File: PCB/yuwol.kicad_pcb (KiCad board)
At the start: 2 copper layers, 172.5 x 122.5 mm, 3 parts

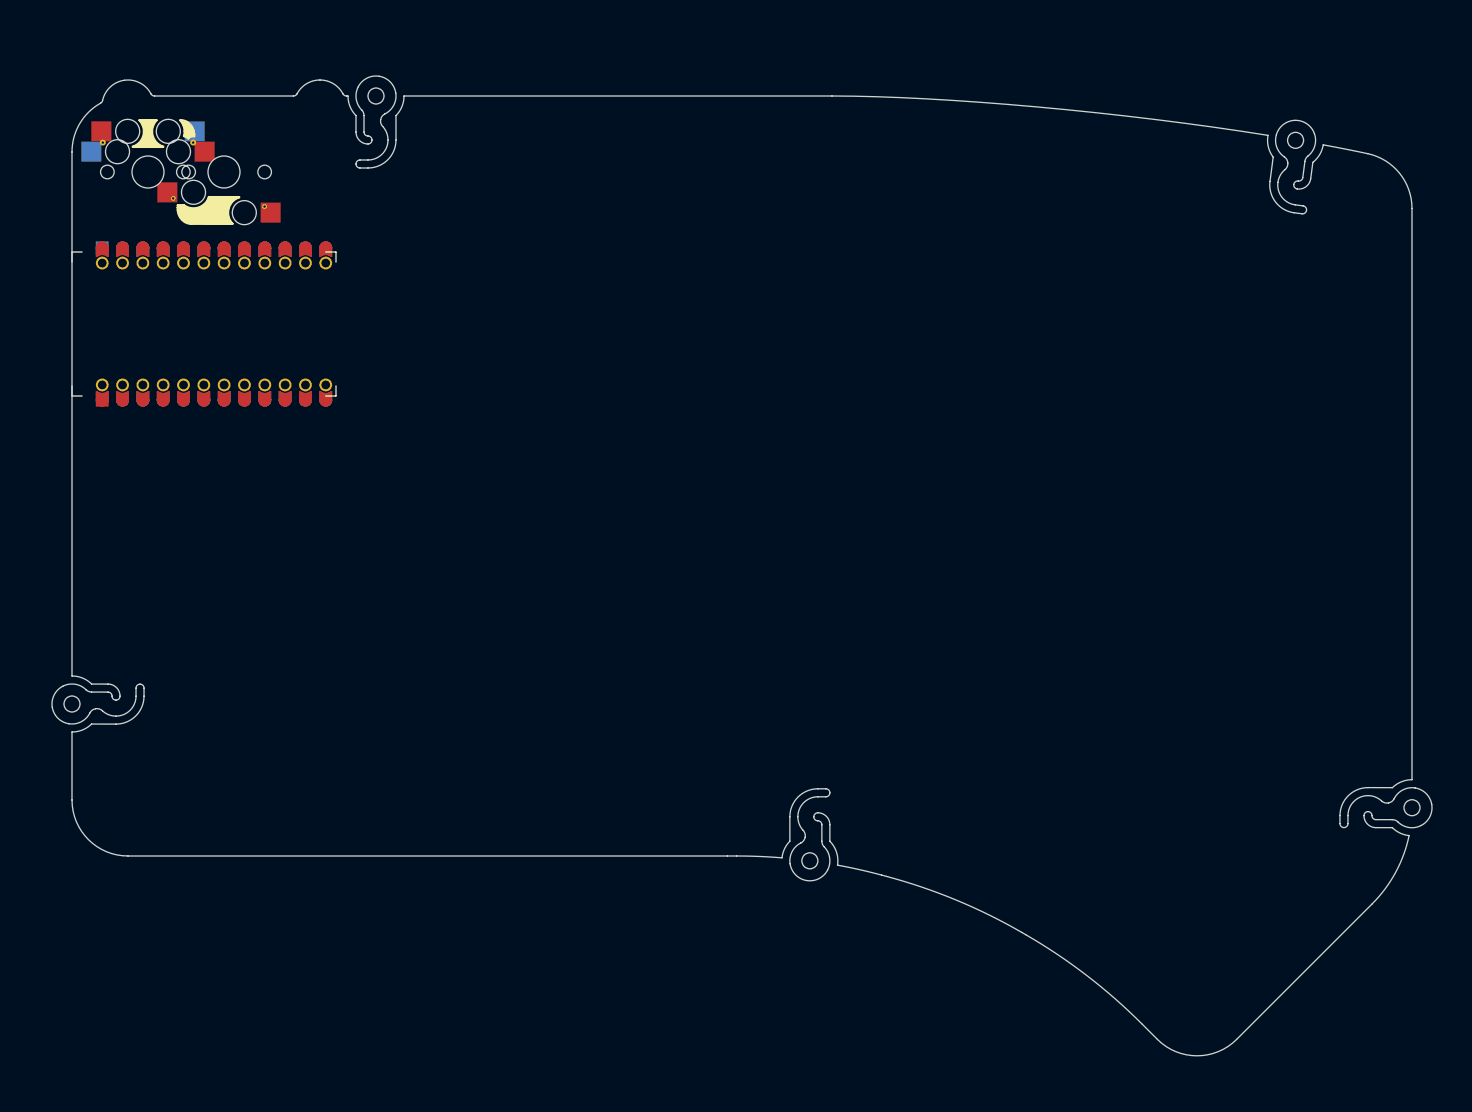
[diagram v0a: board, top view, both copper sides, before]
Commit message: place components
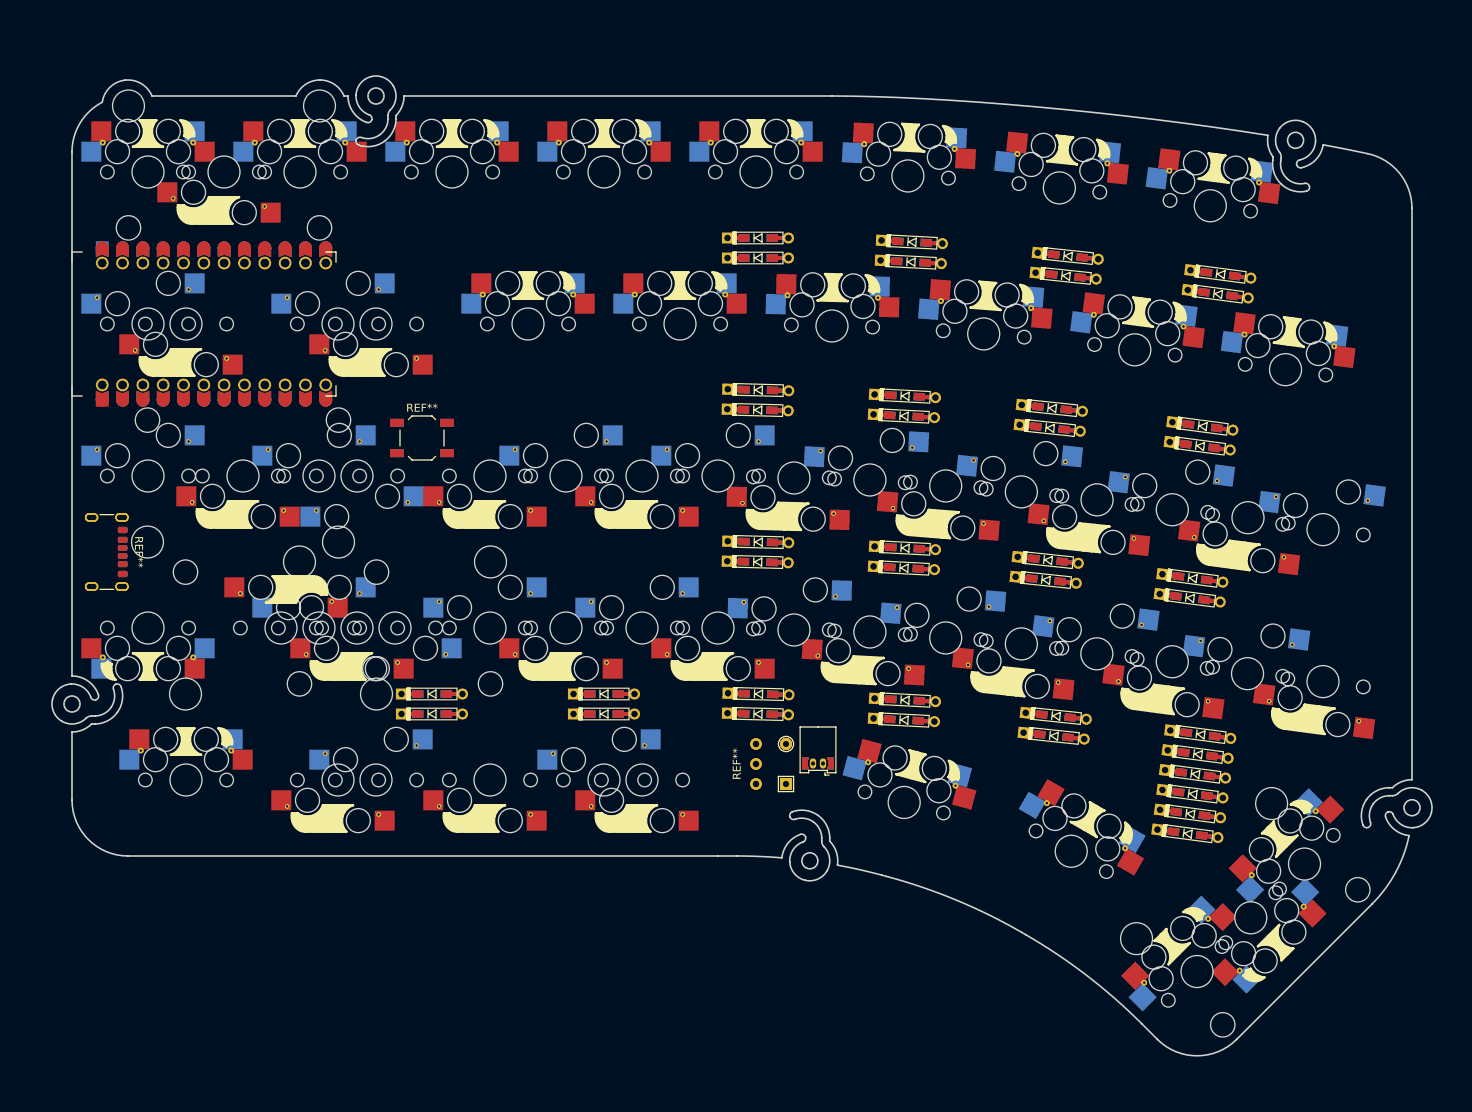
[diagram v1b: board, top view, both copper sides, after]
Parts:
- added REF**: TestPoint_THTPad_D1.5mm_Drill0.7mm, TestPoint:TestPoint_THTPad_D1.5mm_Drill0.7mm, F.Cu at (151.2, 121.0)
- added REF**: D, yubuGadgetsFootpints:Diode_TH_SMD_REVERSIBLE, F.Cu at (184.7, 120.0)
- added REF**: D, yubuGadgetsFootpints:Diode_TH_SMD_REVERSIBLE, F.Cu at (166.0, 118.0)
- added REF**: D, yubuGadgetsFootpints:Diode_TH_SMD_REVERSIBLE, F.Cu at (203.3, 81.3)
- added REF**: D, yubuGadgetsFootpints:Diode_TH_SMD_REVERSIBLE, F.Cu at (202.7, 122.3)
- added REF**: D, yubuGadgetsFootpints:Diode_TH_SMD_REVERSIBLE, F.Cu at (186.2, 62.5)
- added REF**: D, yubuGadgetsFootpints:Diode_TH_SMD_REVERSIBLE, F.Cu at (166.9, 60.7)
- added REF**: D, yubuGadgetsFootpints:Diode_TH_SMD_REVERSIBLE, F.Cu at (147.8, 76.8)
- added REF**: D, yubuGadgetsFootpints:Diode_TH_SMD_REVERSIBLE, F.Cu at (147.8, 60.2)
- added REF**: D, yubuGadgetsFootpints:Diode_TH_SMD_REVERSIBLE, F.Cu at (128.5, 114.8)
- added REF**: StabilizerHole_2u, yubuGadgetsFootpints:StabilizerHole_2u, F.Cu at (88.1, 106.5)
- added REF**: D, yubuGadgetsFootpints:Diode_TH_SMD_REVERSIBLE, F.Cu at (166.1, 115.5)
- added REF**: TestPoint_THTPad_1.5x1.5mm_Drill0.7mm, TestPoint:TestPoint_THTPad_1.5x1.5mm_Drill0.7mm, F.Cu at (151.2, 126.0)
- added REF**: D, yubuGadgetsFootpints:Diode_TH_SMD_REVERSIBLE, F.Cu at (184.0, 98.0)
- added REF**: D, yubuGadgetsFootpints:Diode_TH_SMD_REVERSIBLE, F.Cu at (107.0, 114.8)
- added REF**: D, yubuGadgetsFootpints:Diode_TH_SMD_REVERSIBLE, F.Cu at (183.7, 100.5)
- added REF**: D, yubuGadgetsFootpints:Diode_TH_SMD_REVERSIBLE, F.Cu at (147.8, 57.8)
- added REF**: D, yubuGadgetsFootpints:Diode_TH_SMD_REVERSIBLE, F.Cu at (147.8, 114.8)
- added REF**: D, yubuGadgetsFootpints:Diode_TH_SMD_REVERSIBLE, F.Cu at (107.0, 117.2)
- added REF**: D, yubuGadgetsFootpints:Diode_TH_SMD_REVERSIBLE, F.Cu at (205.6, 62.3)
- added REF**: D, yubuGadgetsFootpints:Diode_TH_SMD_REVERSIBLE, F.Cu at (128.5, 117.2)
- added REF**: D, yubuGadgetsFootpints:Diode_TH_SMD_REVERSIBLE, F.Cu at (147.8, 95.8)
- added REF**: USB_C_Receptacle_GCT_USB4125-xx-x_6P_TopMnt_Horizontal, Connector_USB:USB_C_Receptacle_GCT_USB4125-xx-x_6P_TopMnt_Horizontal, F.Cu at (65.2, 97.0)
- added REF**: D, yubuGadgetsFootpints:Diode_TH_SMD_REVERSIBLE, F.Cu at (185.0, 117.5)
- added REF**: D, yubuGadgetsFootpints:Diode_TH_SMD_REVERSIBLE, F.Cu at (202.4, 124.8)
- added REF**: Molex_PicoBlade_53048-0210_1x02_P1.25mm_Horizontal_Reversib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, yubuGadgetsFootpints:Molex_PicoBlade_53048-0210_1x02_P1.25mm_Horizontal_ReversibleThru, F.Cu at (155.2, 121.8)
- added REF**: D, yubuGadgetsFootpints:Diode_TH_SMD_REVERSIBLE, F.Cu at (203.1, 119.8)
- added REF**: D, yubuGadgetsFootpints:Diode_TH_SMD_REVERSIBLE, F.Cu at (166.0, 80.0)
- added REF**: D, yubuGadgetsFootpints:Diode_TH_SMD_REVERSIBLE, F.Cu at (184.2, 81.5)
- added REF**: D, yubuGadgetsFootpints:Diode_TH_SMD_REVERSIBLE, F.Cu at (147.7, 98.2)
- added REF**: StabilizerHole_2u, yubuGadgetsFootpints:StabilizerHole_2u, F.Cu at (102.4, 106.5)
- added REF**: D, yubuGadgetsFootpints:Diode_TH_SMD_REVERSIBLE, F.Cu at (166.1, 77.5)
- added REF**: D, yubuGadgetsFootpints:Diode_TH_SMD_REVERSIBLE, F.Cu at (166.0, 99.0)
- added REF**: D, yubuGadgetsFootpints:Diode_TH_SMD_REVERSIBLE, F.Cu at (186.5, 60.0)
- added REF**: D, yubuGadgetsFootpints:Diode_TH_SMD_REVERSIBLE, F.Cu at (201.5, 132.2)
- added REF**: D, yubuGadgetsFootpints:Diode_TH_SMD_REVERSIBLE, F.Cu at (147.7, 79.2)
- added REF**: D, yubuGadgetsFootpints:Diode_TH_SMD_REVERSIBLE, F.Cu at (201.8, 129.7)
- added REF**: D, yubuGadgetsFootpints:Diode_TH_SMD_REVERSIBLE, F.Cu at (205.2, 64.8)
- added REF**: SW_SPDT_SS-12D00, yubuGadgetsFootpints:SW_SPDT_SS-12D00, F.Cu at (147.5, 123.5)
- added REF**: StabilizerHole_2u, yubuGadgetsFootpints:StabilizerHole_2u, F.Cu at (81.0, 49.5)
- added REF**: StabilizerHole_2u, yubuGadgetsFootpints:StabilizerHole_2u, F.Cu at (209.3, 142.7)
- added REF**: D, yubuGadgetsFootpints:Diode_TH_SMD_REVERSIBLE, F.Cu at (147.8, 117.2)
- added REF**: D, yubuGadgetsFootpints:Diode_TH_SMD_REVERSIBLE, F.Cu at (201.8, 102.8)
- added REF**: SW_SPST_TL3342, Button_Switch_SMD:SW_SPST_TL3342, F.Cu at (105.8, 82.8)
- added REF**: D, yubuGadgetsFootpints:Diode_TH_SMD_REVERSIBLE, F.Cu at (166.1, 96.5)
- added REF**: D, yubuGadgetsFootpints:Diode_TH_SMD_REVERSIBLE, F.Cu at (203.0, 83.8)
- added REF**: StabilizerHole_2u, yubuGadgetsFootpints:StabilizerHole_2u, F.Cu at (83.4, 87.5)
- added REF**: TestPoint_THTPad_D1.5mm_Drill0.7mm, TestPoint:TestPoint_THTPad_D1.5mm_Drill0.7mm, B.Cu at (151.2, 121.0)
- added REF**: USB_C_Receptacle_GCT_USB4125-xx-x_6P_TopMnt_Horizontal, Connector_USB:USB_C_Receptacle_GCT_USB4125-xx-x_6P_TopMnt_Horizontal, B.Cu at (65.2, 97.0)
- added REF**: TestPoint_THTPad_1.5x1.5mm_Drill0.7mm, TestPoint:TestPoint_THTPad_1.5x1.5mm_Drill0.7mm, B.Cu at (151.2, 126.0)
- added REF**: SW_SPST_TL3342, Button_Switch_SMD:SW_SPST_TL3342, B.Cu at (105.8, 82.8)
- added REF**: D, yubuGadgetsFootpints:Diode_TH_SMD_REVERSIBLE, F.Cu at (202.1, 100.3)
- added REF**: D, yubuGadgetsFootpints:Diode_TH_SMD_REVERSIBLE, F.Cu at (184.5, 79.0)
- added REF**: D, yubuGadgetsFootpints:Diode_TH_SMD_REVERSIBLE, F.Cu at (167.0, 58.2)
- added REF**: D, yubuGadgetsFootpints:Diode_TH_SMD_REVERSIBLE, F.Cu at (202.1, 127.2)
- added S*: Val**, yubuGadgetsFootpints:MX_Hotswap_FootprintPropertyFix_Guided, F.Cu at (204.3, 53.7)
- added S*: Val**, yubuGadgetsFootpints:MX_Hotswap_FootprintPropertyFix_Guided, F.Cu at (186.9, 134.4)
- added S*: Val**, yubuGadgetsFootpints:MX_Hotswap_FootprintPropertyFix_Guided, F.Cu at (71.5, 106.5)
- added S*: Val**, yubuGadgetsFootpints:MX_Hotswap_FootprintPropertyFix_Guided, F.Cu at (176.0, 69.7)
- added S*: Val**, yubuGadgetsFootpints:MX_Hotswap_FootprintPropertyFix_Guided, F.Cu at (166.5, 50.0)
- added S*: Val**, yubuGadgetsFootpints:MX_HotswapOneside_Via_Guided, F.Cu at (180.7, 108.5)
- added S*: Val**, yubuGadgetsFootpints:MX_Hotswap_FootprintPropertyFix_Guided, F.Cu at (157.0, 68.7)
- added S*: Val**, yubuGadgetsFootpints:MX_HotswapOneside_Via_Guided, F.Cu at (171.2, 88.7)
- added S*: Val**, yubuGadgetsFootpints:MX_Hotswap_FootprintPropertyFix_Guided, F.Cu at (90.5, 49.5)
- added S*: Val**, yubuGadgetsFootpints:MX_HotswapOneside_Via_Guided, F.Cu at (123.8, 106.5)
- added S*: Val**, yubuGadgetsFootpints:MX_Hotswap_FootprintPropertyFix_Guided, F.Cu at (213.7, 74.2)
- added S*: Val**, yubuGadgetsFootpints:MX_HotswapOneside_Via_Guided, F.Cu at (114.2, 125.5)
- added S*: Val**, yubuGadgetsFootpints:MX_Hotswap_FootprintPropertyFix_Guided, F.Cu at (138.0, 68.5)
- added S*: Val**, yubuGadgetsFootpints:MX_Hotswap_FootprintPropertyFix_Guided, F.Cu at (76.2, 125.5)
- added S*: Val**, yubuGadgetsFootpints:MX_HotswapOneside_Via_Guided, F.Cu at (76.2, 68.5)
- added S*: Val**, yubuGadgetsFootpints:MX_HotswapOneside_Via_Guided, F.Cu at (190.1, 90.5)
- added S*: Val**, yubuGadgetsFootpints:MX_HotswapOneside_Via_Guided, F.Cu at (218.4, 113.2)
- added S*: Val**, yubuGadgetsFootpints:MX_Hotswap_FootprintPropertyFix_Guided, F.Cu at (209.3, 142.7)
- added S*: Val**, yubuGadgetsFootpints:MX_HotswapOneside_Via_Guided, F.Cu at (142.8, 106.5)
- added S*: Val**, yubuGadgetsFootpints:MX_HotswapOneside_Via_Guided, F.Cu at (152.2, 87.7)
- added S*: Val**, yubuGadgetsFootpints:MX_Hotswap_FootprintPropertyFix_Guided, F.Cu at (202.6, 149.4)
- added S*: Val**, yubuGadgetsFootpints:MX_HotswapOneside_Via_Guided, F.Cu at (97.6, 106.5)
- added S*: Val**, yubuGadgetsFootpints:MX_HotswapOneside_Via_Guided, F.Cu at (209.0, 92.7)
- added S*: Val**, yubuGadgetsFootpints:MX_Hotswap_FootprintPropertyFix_Guided, F.Cu at (119.0, 68.5)
- added S*: Val**, yubuGadgetsFootpints:MX_Hotswap_FootprintPropertyFix_Guided, F.Cu at (166.0, 128.3)
- added S*: Val**, yubuGadgetsFootpints:MX_HotswapOneside_Via_Guided, F.Cu at (133.2, 125.5)
- added S*: Val**, yubuGadgetsFootpints:MX_HotswapOneside_Via_Guided, F.Cu at (88.1, 106.5)
- added S*: Val**, yubuGadgetsFootpints:MX_Hotswap_FootprintPropertyFix_Guided, F.Cu at (147.5, 49.5)
- added S*: Val**, yubuGadgetsFootpints:MX_HotswapOneside_Via_Guided, F.Cu at (199.5, 110.7)
- added S*: Val**, yubuGadgetsFootpints:MX_Hotswap_FootprintPropertyFix_Guided, F.Cu at (128.5, 49.5)
- added S*: Val**, yubuGadgetsFootpints:MX_Hotswap_FootprintPropertyFix_Guided, F.Cu at (216.1, 136.0)
- added S*: Val**, yubuGadgetsFootpints:MX_HotswapOneside_Via_Guided, F.Cu at (114.2, 87.5)
- added S*: Val**, yubuGadgetsFootpints:MX_HotswapOneside_Via_Guided, F.Cu at (100.0, 68.5)
- added S*: Val**, yubuGadgetsFootpints:MX_Hotswap_FootprintPropertyFix_Guided, F.Cu at (185.4, 51.5)
- added S*: Val**, yubuGadgetsFootpints:MX_Hotswap_FootprintPropertyFix_Guided, F.Cu at (109.5, 49.5)
- added S*: Val**, yubuGadgetsFootpints:MX_HotswapOneside_Via_Guided, B.Cu at (208.9, 112.2)
- added S*: Val**, yubuGadgetsFootpints:MX_HotswapOneside_Via_Guided, B.Cu at (171.2, 107.7)
- added S*: Val**, yubuGadgetsFootpints:MX_HotswapOneside_Via_Guided, B.Cu at (100.0, 125.5)
- added S*: Val**, yubuGadgetsFootpints:MX_HotswapOneside_Via_Guided, B.Cu at (199.5, 91.7)
- added S*: Val**, yubuGadgetsFootpints:MX_HotswapOneside_Via_Guided, B.Cu at (114.2, 106.5)
- added S*: Val**, yubuGadgetsFootpints:MX_HotswapOneside_Via_Guided, B.Cu at (128.5, 125.5)
- added S*: Val**, yubuGadgetsFootpints:MX_HotswapOneside_Via_Guided, B.Cu at (190.1, 109.7)
- added S*: Val**, yubuGadgetsFootpints:MX_HotswapOneside_Via_Guided, F.Cu at (133.2, 87.5)
- added S*: Val**, yubuGadgetsFootpints:MX_HotswapOneside_Via_Guided, B.Cu at (133.2, 106.5)
- added S*: Val**, yubuGadgetsFootpints:MX_HotswapOneside_Via_Guided, B.Cu at (218.4, 94.2)
- added S*: Val**, yubuGadgetsFootpints:MX_HotswapOneside_Via_Guided, B.Cu at (102.4, 106.5)
- added S*: Val**, yubuGadgetsFootpints:MX_HotswapOneside_Via_Guided, B.Cu at (152.2, 106.7)
- added S*: Val**, yubuGadgetsFootpints:MX_HotswapOneside_Via_Guided, B.Cu at (161.7, 88.0)
- added S*: Val**, yubuGadgetsFootpints:MX_HotswapOneside_Via_Guided, B.Cu at (180.7, 89.5)
- added S*: Val**, yubuGadgetsFootpints:MX_HotswapOneside_Via_Guided, B.Cu at (123.8, 87.5)
- added S*: Val**, yubuGadgetsFootpints:MX_HotswapOneside_Via_Guided, B.Cu at (92.9, 106.5)
- added S*: Val**, yubuGadgetsFootpints:MX_HotswapOneside_Via_Guided, B.Cu at (71.5, 87.5)
- added S*: Val**, yubuGadgetsFootpints:MX_HotswapOneside_Via_Guided, B.Cu at (92.9, 87.5)
- added S*: Val**, yubuGadgetsFootpints:MX_HotswapOneside_Via_Guided, F.Cu at (95.2, 125.5)
- added S*: Val**, yubuGadgetsFootpints:MX_HotswapOneside_Via_Guided, B.Cu at (71.5, 68.5)
- added S*: Val**, yubuGadgetsFootpints:MX_HotswapOneside_Via_Guided, B.Cu at (97.6, 87.5)
- added S*: Val**, yubuGadgetsFootpints:MX_HotswapOneside_Via_Guided, B.Cu at (95.2, 68.5)
- added S*: Val**, yubuGadgetsFootpints:MX_HotswapOneside_Via_Guided, B.Cu at (142.8, 87.5)
- added S*: Val**, yubuGadgetsFootpints:MX_HotswapOneside_Via_Guided, F.Cu at (161.7, 107.0)
- added S*: Val**, yubuGadgetsFootpints:MX_Hotswap_FootprintPropertyFix_Guided, F.Cu at (194.9, 71.7)
- added S*: Val**, yubuGadgetsFootpints:MX_HotswapOneside_Via_Guided, F.Cu at (83.4, 87.5)
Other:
- outline, holes or cut-outs redrawn

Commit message: fix pcb data
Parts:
- added JP1: SolderJumper-2_P1.3mm_Open_TrianglePad1.0x1.5mm, Jumper:SolderJumper-2_P1.3mm_Open_TrianglePad1.0x1.5mm, B.Cu at (114.2, 120.5)
- moved REF** 0.95 mm to (203.0, 127.4)
- moved REF** 0.95 mm to (203.7, 122.5)
- moved REF** 0.95 mm to (204.0, 120.0)
- moved REF** 0.95 mm to (202.4, 132.4)
- moved REF** 0.95 mm to (202.7, 129.9)
- moved REF** 0.95 mm to (203.3, 125.0)
- renumbered REF** to J1, REF** to J3, REF** to SW41, REF** to SW42, REF** to TP+1, REF** to TP-1, REF** to U1
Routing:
- added copper zone on B.Cu, net GND
- added copper zone on F.Cu, net GND
